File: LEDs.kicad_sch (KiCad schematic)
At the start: 13 parts, among them U16 SN74LVC244A

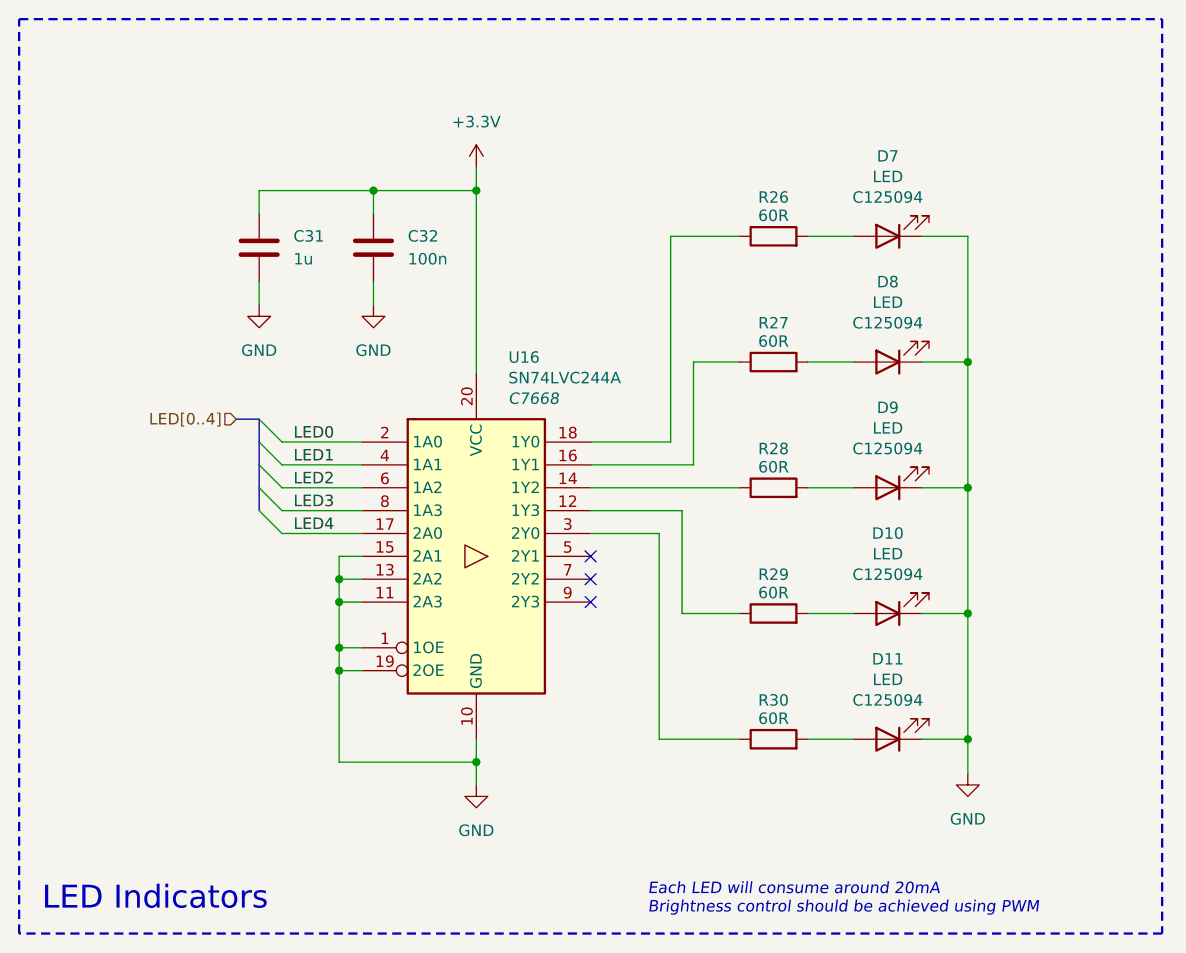
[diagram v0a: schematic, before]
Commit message: display driver update
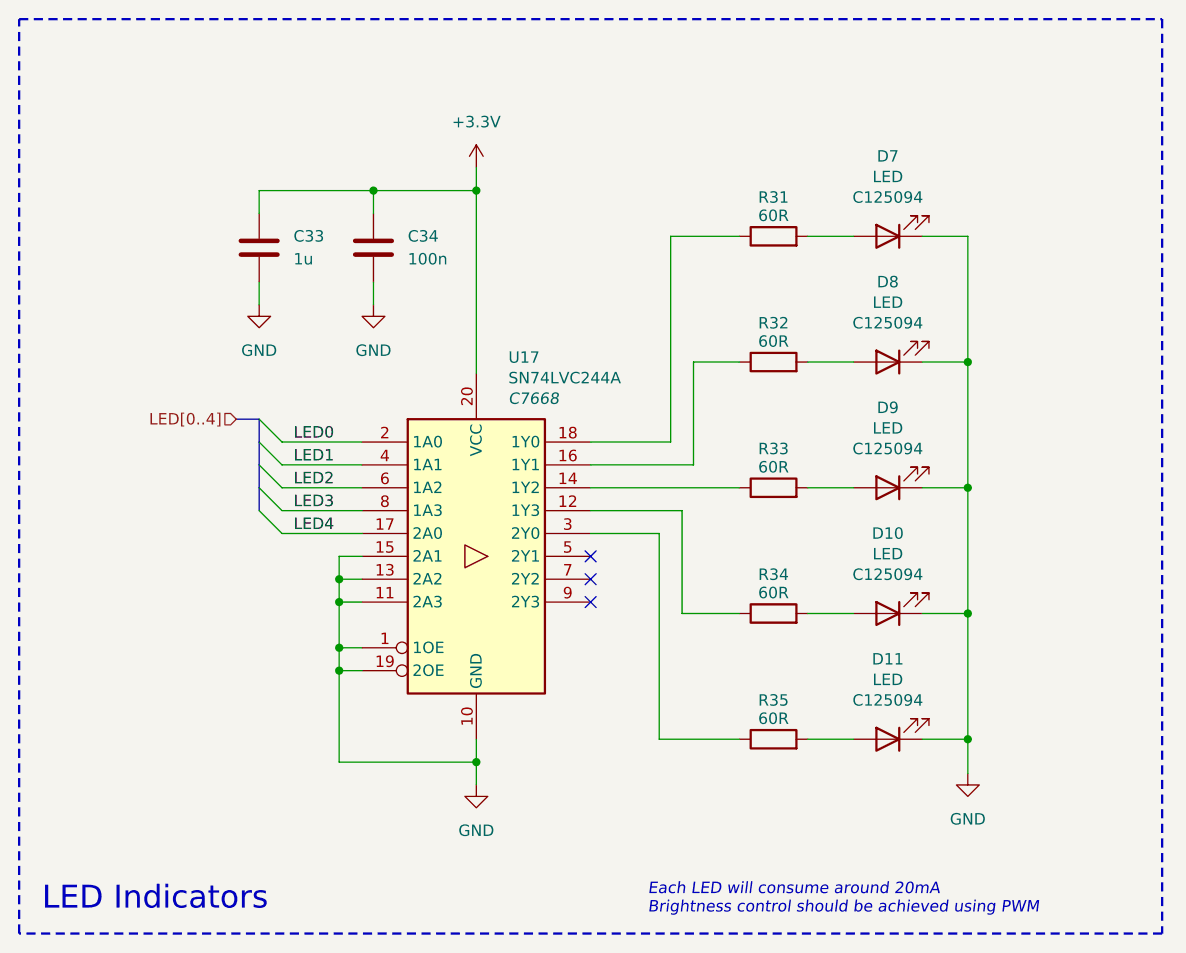
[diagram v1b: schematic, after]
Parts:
- renumbered C31 to C33, C32 to C34, R26 to R31, R27 to R32, R28 to R33, R29 to R34, R30 to R35, U16 to U17
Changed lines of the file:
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@@
 		(on_board yes)
 		(dnp no)
-		(property "Reference" "R27"
+		(property "Reference" "R32"
 			(at 160.02 78.232 90)
 			(effects
@@
 			(project "Precision Clock"
 				(path "/c9a8ff63-a0d1-4125-9dd1-40fb53daf536/7feba6ed-769c-49aa-8cad-0f57dc62b971"
-					(reference "R27")
+					(reference "R32")
 					(unit 1)
 				)
@@
 		(dnp no)
 		(fields_autoplaced yes)
-		(property "Reference" "#PWR085"
+		(property "Reference" "#PWR091"
 			(at 127 135.89 0)
 			(effects
@@
 			(project "Precision Clock"
 				(path "/c9a8ff63-a0d1-4125-9dd1-40fb53daf536/7feba6ed-769c-49aa-8cad-0f57dc62b971"
-					(reference "#PWR085")
+					(reference "#PWR091")
 					(unit 1)
 				)
@@
 		(on_board yes)
 		(dnp no)
-		(property "Reference" "R30"
+		(property "Reference" "R35"
 			(at 160.02 120.142 90)
 			(effects
@@
 			(project "Precision Clock"
 				(path "/c9a8ff63-a0d1-4125-9dd1-40fb53daf536/7feba6ed-769c-49aa-8cad-0f57dc62b971"
-					(reference "R30")
+					(reference "R35")
 					(unit 1)
 				)
@@
 		(dnp no)
 		(fields_autoplaced yes)
-		(property "Reference" "#PWR082"
+		(property "Reference" "#PWR088"
 			(at 102.87 82.55 0)
 			(effects
@@
 			(project "Precision Clock"
 				(path "/c9a8ff63-a0d1-4125-9dd1-40fb53daf536/7feba6ed-769c-49aa-8cad-0f57dc62b971"
-					(reference "#PWR082")
+					(reference "#PWR088")
 					(unit 1)
 				)
@@
 		(dnp no)
 		(fields_autoplaced yes)
-		(property "Reference" "#PWR083"
+		(property "Reference" "#PWR089"
 			(at 115.57 82.55 0)
 			(effects
@@
 			(project "Precision Clock"
 				(path "/c9a8ff63-a0d1-4125-9dd1-40fb53daf536/7feba6ed-769c-49aa-8cad-0f57dc62b971"
-					(reference "#PWR083")
+					(reference "#PWR089")
 					(unit 1)
 				)
@@
 		(on_board yes)
 		(dnp no)
-		(property "Reference" "R29"
+		(property "Reference" "R34"
 			(at 160.02 106.172 90)
 			(effects
@@
 			(project "Precision Clock"
 				(path "/c9a8ff63-a0d1-4125-9dd1-40fb53daf536/7feba6ed-769c-49aa-8cad-0f57dc62b971"
-					(reference "R29")
+					(reference "R34")
 					(unit 1)
 				)
@@
 		(dnp no)
 		(fields_autoplaced yes)
-		(property "Reference" "C32"
+		(property "Reference" "C34"
 			(at 119.38 68.5799 0)
 			(effects
@@
 			(project "Precision Clock"
 				(path "/c9a8ff63-a0d1-4125-9dd1-40fb53daf536/7feba6ed-769c-49aa-8cad-0f57dc62b971"
-					(reference "C32")
+					(reference "C34")
 					(unit 1)
 				)
@@
 		(on_board yes)
 		(dnp no)
-		(property "Reference" "U16"
+		(property "Reference" "U17"
 			(at 130.556 82.042 0)
 			(effects
@@
 			(project "Precision Clock"
 				(path "/c9a8ff63-a0d1-4125-9dd1-40fb53daf536/7feba6ed-769c-49aa-8cad-0f57dc62b971"
-					(reference "U16")
+					(reference "U17")
 					(unit 1)
 				)
@@
 		(on_board yes)
 		(dnp no)
-		(property "Reference" "R28"
+		(property "Reference" "R33"
 			(at 160.02 92.202 90)
 			(effects
@@
 			(project "Precision Clock"
 				(path "/c9a8ff63-a0d1-4125-9dd1-40fb53daf536/7feba6ed-769c-49aa-8cad-0f57dc62b971"
-					(reference "R28")
+					(reference "R33")
 					(unit 1)
 				)
@@
 		(on_board yes)
 		(dnp no)
-		(property "Reference" "R26"
+		(property "Reference" "R31"
 			(at 160.02 64.262 90)
 			(effects
@@
 			(project "Precision Clock"
 				(path "/c9a8ff63-a0d1-4125-9dd1-40fb53daf536/7feba6ed-769c-49aa-8cad-0f57dc62b971"
-					(reference "R26")
+					(reference "R31")
 					(unit 1)
 				)
@@
 		(dnp no)
 		(fields_autoplaced yes)
-		(property "Reference" "C31"
+		(property "Reference" "C33"
 			(at 106.68 68.5799 0)
 			(effects
@@
 			(project "Precision Clock"
 				(path "/c9a8ff63-a0d1-4125-9dd1-40fb53daf536/7feba6ed-769c-49aa-8cad-0f57dc62b971"
-					(reference "C31")
+					(reference "C33")
 					(unit 1)
 				)
@@
 		(dnp no)
 		(fields_autoplaced yes)
-		(property "Reference" "#PWR084"
+		(property "Reference" "#PWR090"
 			(at 127 64.77 0)
 			(effects
@@
 			(project "Precision Clock"
 				(path "/c9a8ff63-a0d1-4125-9dd1-40fb53daf536/7feba6ed-769c-49aa-8cad-0f57dc62b971"
-					(reference "#PWR084")
+					(reference "#PWR090")
 					(unit 1)
 				)
@@
 		(dnp no)
 		(fields_autoplaced yes)
-		(property "Reference" "#PWR086"
+		(property "Reference" "#PWR092"
 			(at 181.61 134.62 0)
 			(effects
@@
 			(project "Precision Clock"
 				(path "/c9a8ff63-a0d1-4125-9dd1-40fb53daf536/7feba6ed-769c-49aa-8cad-0f57dc62b971"
-					(reference "#PWR086")
-					(unit 1)
-				)
+					(reference "#PWR092")
+					(unit 1)
+				)
